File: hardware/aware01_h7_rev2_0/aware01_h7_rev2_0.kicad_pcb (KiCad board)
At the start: 4 copper layers, 46 x 110 mm, 161 parts, among them IC1 TLV320AIC3204IRHBR, IC2 587-2054-127F, IC3 587-2054-127F, IC4 587-2054-127F, IC5 587-2054-127F, J1 CV3_IN, J10 CV2_IN, J11 V/OCT_IN, J12 CV1_IN, J13 GATE3_IN, J14 GATE4_IN, J2 Conn_02x07_Odd_Even, J3 Conn_02x05_Odd_Even, J4 InL, J5 InR, J6 OutL, J7 OutR, J8 GATE1_IN, J9 GATE2_IN, Q1 MMBT3904, Q2 MMBT3904, Q3 MMBT3904, Q4 MMBT3904, SW2 SW_Push, SW3 SW_Push, U1 LMR50410Y5FQDBVRQ1, U10 NE5532DRG4, U11 LMV722IDR, U12 LMV722IDR, U2 STM32H7A3RITx, U3 10k, U4 10k, U5 10k, U6 10k, U7 LM1117MP-3.3, U8 LM4040DIM3X-10, U9 NE5532DRG4, Y2 WE-XTAL 24.0MHz 50ppm

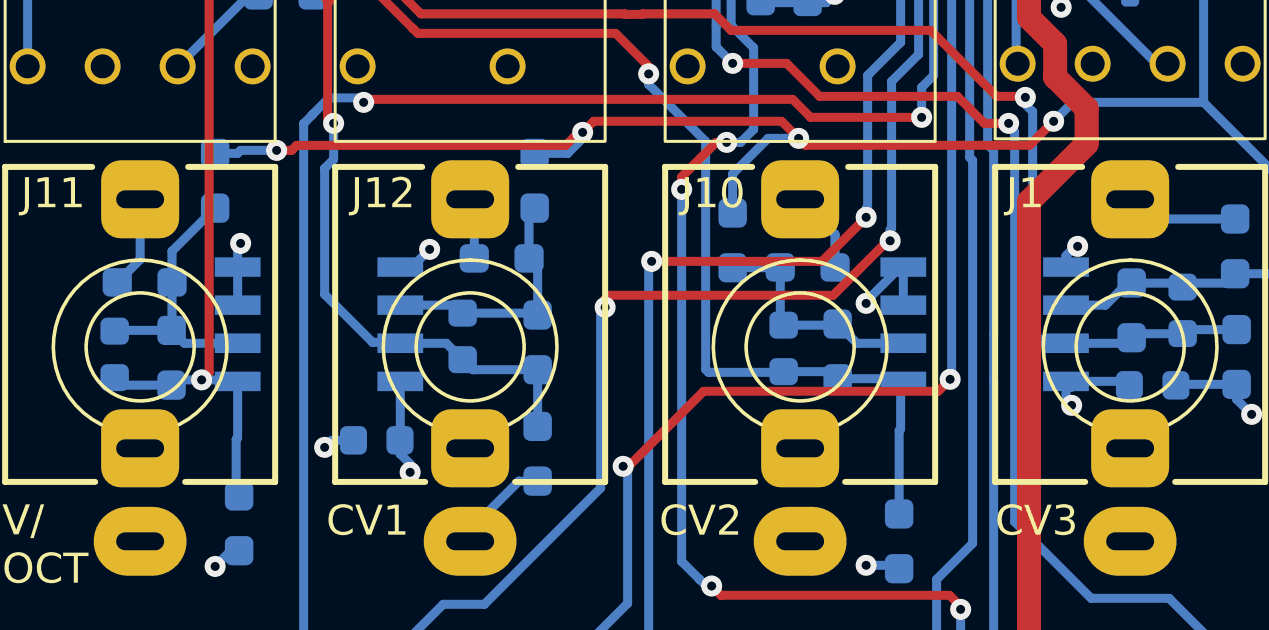
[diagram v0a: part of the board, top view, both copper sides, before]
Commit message: hwardware: update analog stages simulation
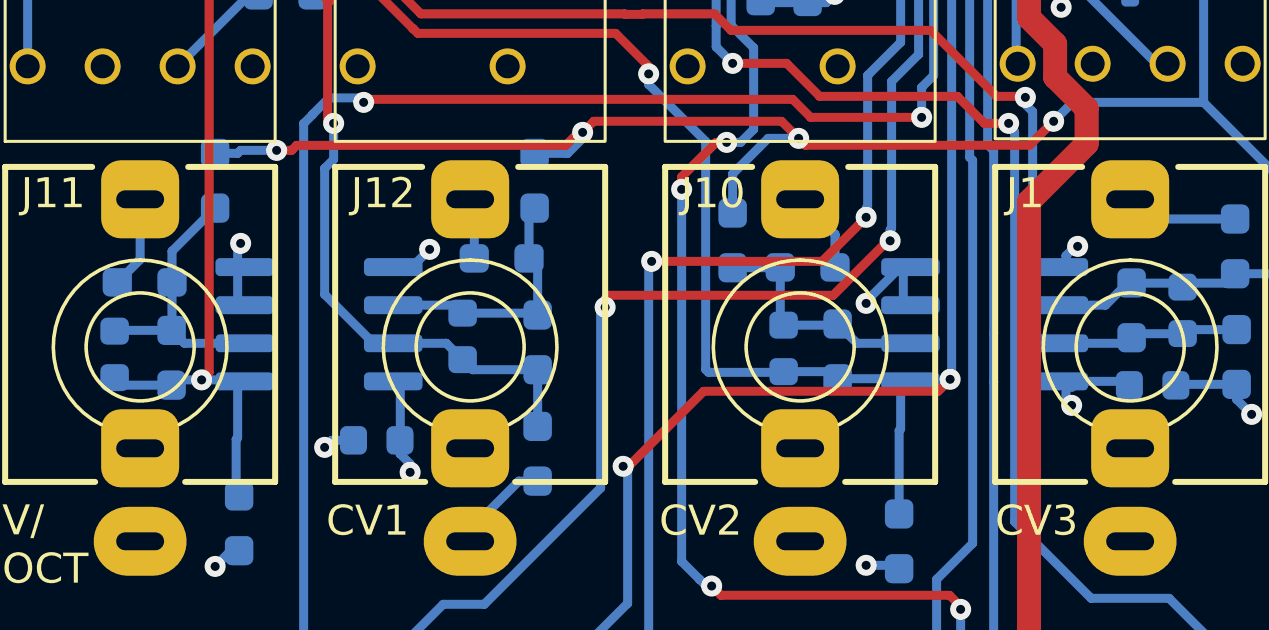
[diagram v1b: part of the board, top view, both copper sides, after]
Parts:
- U11, U12: value LMV722IDR -> OPA2322AIDR; footprint Eurorack:LMV722IDR -> Package_SO:SOIC-8_3.9x4.9mm_P1.27mm

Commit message: hardware: update analog sim and routing (wip)
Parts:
- removed the C50 at (137.8, 146.4)
- removed the C51 at (147.2, 144.6)
- removed the C56 at (164.1, 136.1)
- removed the C57 at (173.5, 136.1)
- removed the C58 at (159.4, 145.7)
- removed the C59 at (168.8, 144.3)
- removed the R11 at (173.2, 113.6)
- removed R48, R49, R58, R59: 22k, Resistor_SMD:R_0603_1608Metric_Pad0.98x0.95mm_HandSolder
- removed R50, R51, R56, R57: 3.3k, Resistor_SMD:R_0603_1608Metric_Pad0.98x0.95mm_HandSolder
- removed R52, R53, R60, R61: 1k, Resistor_SMD:R_0603_1608Metric_Pad0.98x0.95mm_HandSolder
- removed R54, R55, R69, R76, R77: 100k, Resistor_SMD:R_0603_1608Metric_Pad0.98x0.95mm_HandSolder
- added C49: 2.2u, Capacitor_SMD:CP_Elec_4x5.4, B.Cu at (153.7, 133.8)
- added C5: 10u, Capacitor_SMD:C_0603_1608Metric, B.Cu at (121.0, 136.7)
- added C52: 10u, Capacitor_SMD:CP_Elec_4x5.4, B.Cu at (164.1, 136.1)
- added C54: 18p, Capacitor_SMD:C_0603_1608Metric, B.Cu at (120.8, 120.0)
- added C55: 18p, Capacitor_SMD:C_0603_1608Metric, B.Cu at (117.8, 116.5)
- added C9: 10u, Capacitor_SMD:C_0603_1608Metric, B.Cu at (121.0, 139.2)
- added D4: BAT54S, Package_TO_SOT_SMD:SOT-23, B.Cu at (142.4, 138.8)
- added D5: BAT54S, Package_TO_SOT_SMD:SOT-23, B.Cu at (153.8, 139.3)
- added D6: BAT54A, Package_TO_SOT_SMD:SOT-23, B.Cu at (141.3, 127.7)
- added D7: BAT54A, Package_TO_SOT_SMD:SOT-23, B.Cu at (165.6, 129.9)
- added R14: 12k, Resistor_SMD:R_0603_1608Metric_Pad0.98x0.95mm_HandSolder, B.Cu at (114.9, 141.7)
- added R15: 12k, Resistor_SMD:R_0603_1608Metric_Pad0.98x0.95mm_HandSolder, B.Cu at (114.9, 136.7)
- added R16: 1.8k, Resistor_SMD:R_0603_1608Metric_Pad0.98x0.95mm_HandSolder, B.Cu at (114.9, 139.2)
- added R17: 1.8k, Resistor_SMD:R_0603_1608Metric_Pad0.98x0.95mm_HandSolder, B.Cu at (114.9, 134.2)
- added R18: 5.6k, Resistor_SMD:R_0603_1608Metric_Pad0.98x0.95mm_HandSolder, B.Cu at (118.1, 125.3)
- added R19: 5.6k, Resistor_SMD:R_0603_1608Metric_Pad0.98x0.95mm_HandSolder, B.Cu at (115.8, 116.9)
- added R20: 39k, Resistor_SMD:R_0603_1608Metric_Pad0.98x0.95mm_HandSolder, B.Cu at (120.8, 124.4)
- added R21: 39k, Resistor_SMD:R_0603_1608Metric_Pad0.98x0.95mm_HandSolder, B.Cu at (116.7, 114.0)
- added R22: 1k, Resistor_SMD:R_0603_1608Metric_Pad0.98x0.95mm_HandSolder, B.Cu at (121.9, 127.0)
- added R23: 1k, Resistor_SMD:R_0603_1608Metric_Pad0.98x0.95mm_HandSolder, B.Cu at (108.8, 107.5)
- added U3: LM1117MP-1.8, Package_TO_SOT_SMD:SOT-223-3_TabPin2, B.Cu at (153.2, 147.2)
- C53: value 2.2u -> 10u
- moved C53 19.8 mm to (173.3, 136.3), turned to -90 degrees
- moved R28 5.05 mm to (139.8, 123.5), turned to 90 degrees
- moved C48 2.83 mm to (142.3, 133.2), turned to -90 degrees
- moved R31 2.68 mm to (166.1, 126.0), turned to 0 degrees
- renumbered C18 to C1, C7 to C10, C38 to C11, C39 to C12, C25 to C13, C20 to C14, C21 to C15, C24 to C16, C12 to C17, C26 to C18, C1 to C19, C6 to C2, C10 to C20, C13 to C21, C29 to C22, C2 to C23, C14 to C24, C11 to C25, C40 to C26, C32 to C27, C16 to C28, C17 to C29, C19 to C3, C31 to C30, C34 to C31, C3 to C32, C5 to C33, C35 to C34, C27 to C35, C28 to C36, C41 to C37, C42 to C38, C43 to C39, C30 to C4, C44 to C40, C45 to C41, C46 to C42, C8 to C43, C9 to C44, C47 to C45, C48 to C46, C49 to C47, C52 to C48, C54 to C50, C55 to C51, C60 to C56, C61 to C57, C15 to C58, C62 to C59, C22 to C6, C63 to C60, C64 to C61, C23 to C7, C33 to C8, D3 to D1, D1 to D2, D2 to D3, IC5 to IC1, IC4 to IC2, IC2 to IC4, IC1 to IC5, J2 to J1, J14 to J10, J10 to J11, J1 to J12, J11 to J13, J12 to J14, J3 to J2, J4 to J3, J5 to J4, J6 to J5, J7 to J6, J8 to J7, J9 to J8, J13 to J9, L2 to L1, R46 to R1, R42 to R10, R43 to R11, R44 to R12, R45 to R13, R3 to R2, R62 to R24, R63 to R25, R78 to R26, R12 to R27, R64 to R28, R65 to R29, R2 to R3, R79 to R30, R13 to R31, R66 to R32, R67 to R33, R8 to R34, R9 to R35, R68 to R36, R10 to R37, R70 to R38, R71 to R39, R1 to R4, R72 to R40, R73 to R41, R74 to R42, R75 to R43, R80 to R5, R81 to R6, R47 to R7, R40 to R8, R41 to R9, SW2 to SW1, SW3 to SW2, TP5 to TP1, TP4 to TP2, TP2 to TP4, TP1 to TP5, U9 to U10, U10 to U11, U11 to U12, U12 to U13, U7 to U2, U2 to U4, U8 to U5, U3 to U6, U4 to U7, U5 to U8, U6 to U9, Y2 to Y1
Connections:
- C48 pad 1: Net-(C50-Pad1) -> /Audio Codec/Input Output Channels/INL
- C48 pad 2: /Audio Codec/Input Output Channels/INL -> Net-(C48-Pad2)
- C53 pad 1: Net-(C51-Pad1) -> /Audio Codec/Input Output Channels/OUTR
- C53 pad 2: /Audio Codec/Input Output Channels/INR -> Net-(C53-Pad2)
- J3 pad T: Net-(J4-PadT) -> Net-(U10A-+)
- J4 pad T: Net-(J5-PadT) (its old number) -> Net-(U10B-+)
- J4 pad TN: Net-(J4-PadT) -> Net-(U10A-+)
- U10 pad 1: Net-(C50-Pad1) -> Net-(U10A--)
- U10 pad 2: Net-(U9A--) -> Net-(U10A--)
- U10 pad 3: GND -> Net-(U10A-+)
- U10 pad 5: GND -> Net-(U10B-+)
- U10 pad 6: Net-(U9B--) -> Net-(U10B--)
- U10 pad 7: Net-(C51-Pad1) -> Net-(U10B--)
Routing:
- net Net-(U10A-+): track 0.00 -> 19.8 mm
- net Net-(J4-PadT): track 19.8 -> 0.00 mm
- net Net-(C51-Pad1): track 15.3 -> 0.00 mm
- net Net-(C50-Pad1): track 15.2 -> 0.00 mm
- net Net-(C56-Pad1): track 14.3 -> 0.00 mm
- net Net-(U10A--): track 0.00 -> 11.9 mm
- net Net-(C52-Pad2): track 0.00 -> 10.5 mm
- net Net-(U10B--): track 0.00 -> 10.3 mm
- net Net-(Q3-B): track 2.30 -> 10.9 mm, vias 0 -> 2
- net Net-(U12B--): track 7.94 -> 0.00 mm
- net Net-(U11B--): track 5.81 -> 13.7 mm
- net Net-(C57-Pad1): track 6.18 -> 0.00 mm
- net Net-(C53-Pad2): track 0.00 -> 6.18 mm
- net Net-(U9A--): track 5.79 -> 0.00 mm
- net Net-(U9B--): track 5.60 -> 0.00 mm
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
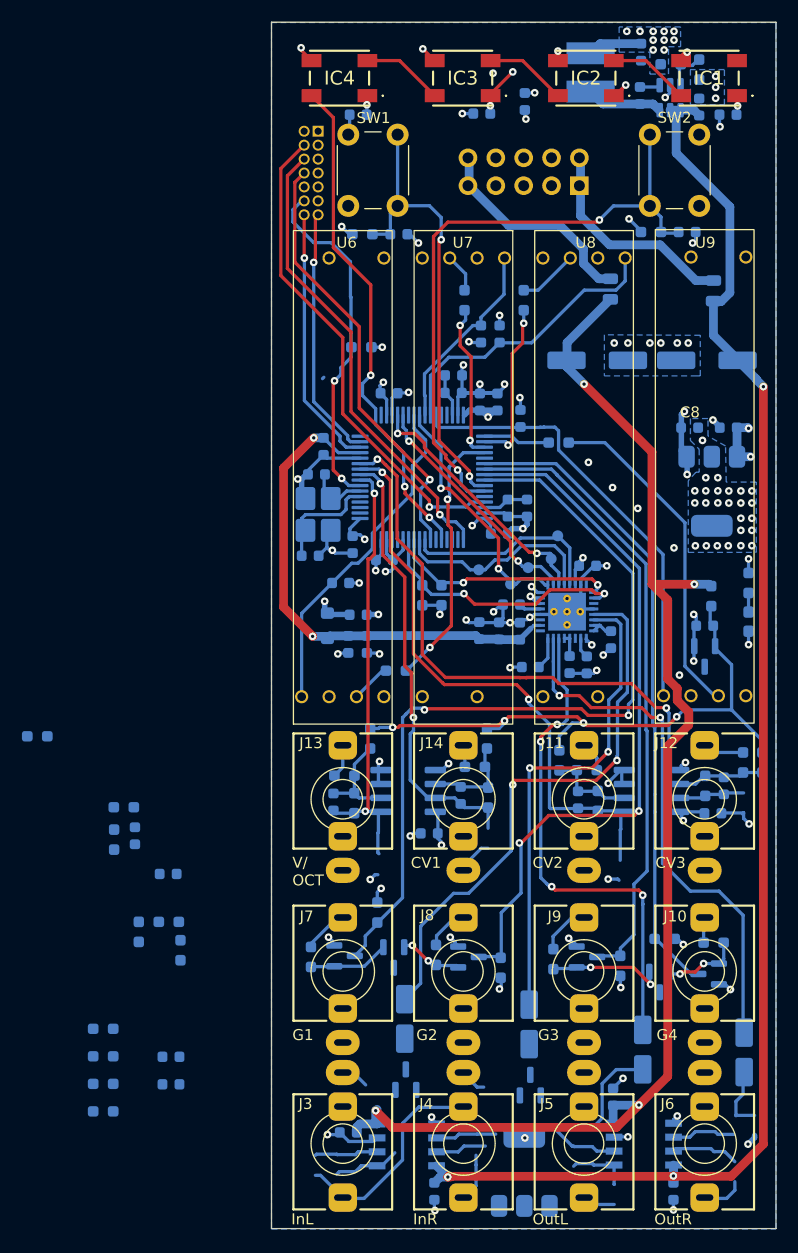
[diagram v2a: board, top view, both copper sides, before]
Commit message: hardware: update layout
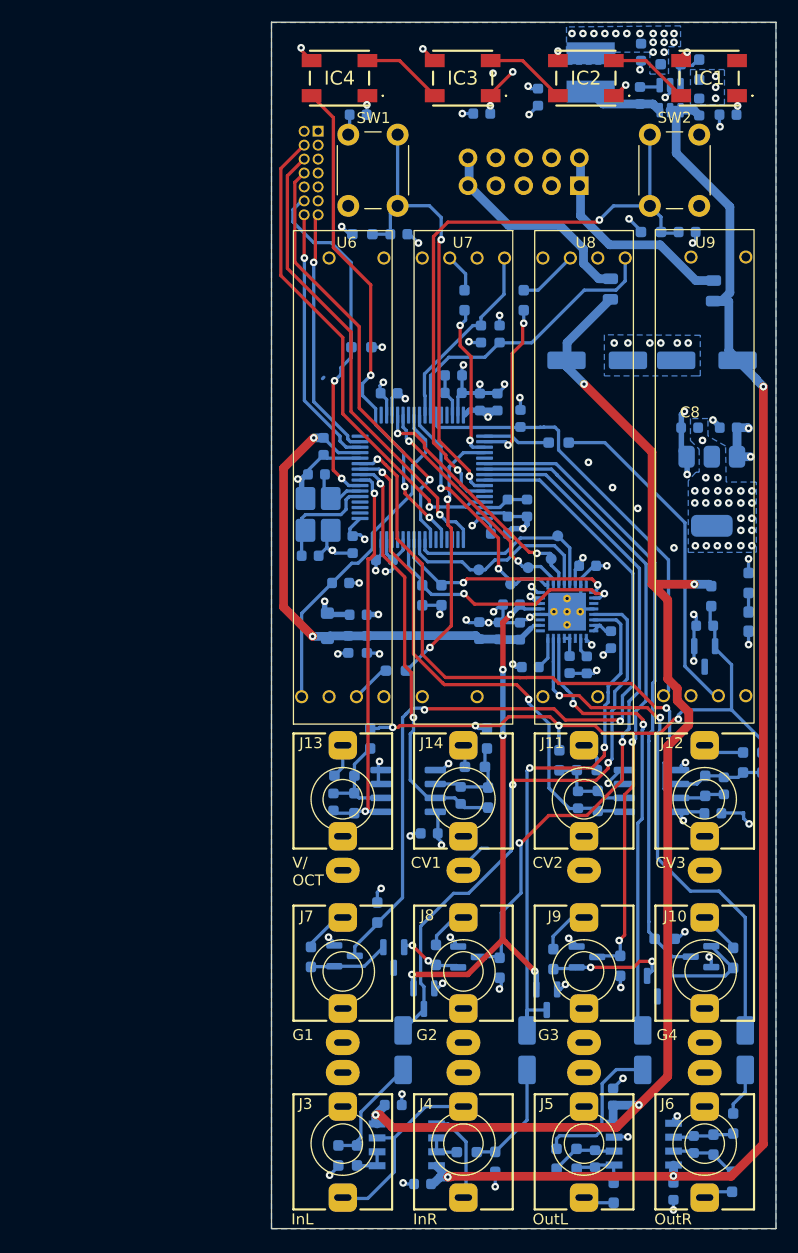
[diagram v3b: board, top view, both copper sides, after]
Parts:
- removed C5, C9: 10u, Capacitor_SMD:C_0603_1608Metric
- removed U3: LM1117MP-1.8, Package_TO_SOT_SMD:SOT-223-3_TabPin2
- moved R23 75.3 mm to (172.2, 148.1), turned to -90 degrees
- moved R19 62.1 mm to (172.3, 142.8), turned to -90 degrees
- moved R21 61.9 mm to (170.5, 144.7), turned to -90 degrees
- moved C55 58.2 mm to (168.7, 144.7), turned to -90 degrees
- moved C54 46.8 mm to (159.7, 146.0), turned to -90 degrees
- moved R22 45.3 mm to (161.4, 149.1)
- moved R18 43.7 mm to (157.1, 145.1), turned to 0 degrees
- moved R20 42.7 mm to (157.1, 146.9)
- moved R17 37.7 mm to (150.6, 146.3), turned to 90 degrees
- moved R15 34.3 mm to (148.0, 145.4)
- moved R14 23.5 mm to (138.0, 145.7), turned to 90 degrees
- moved R16 22.4 mm to (136.3, 145.7), turned to 90 degrees
- moved D5 7.93 mm to (155.3, 131.5), turned to -90 degrees
- moved D4 7.57 mm to (144.1, 131.4), turned to -90 degrees
- moved C47 4.80 mm to (141.3, 141.1), turned to 0 degrees
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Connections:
- C38 pad 2: Net-(IC5-DVDD) -> DVDD
- D4 pad 1: +1V8 -> DVDD
- D5 pad 1: +1V8 -> DVDD
- IC5 pad 29: Net-(IC5-DVDD) -> DVDD
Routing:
- net DVDD: track 0.00 -> 49.9 mm, vias 0 -> 5
- net Net-(C48-Pad2): track 0.00 -> 10.4 mm
- net Net-(C49-Pad2): track 0.00 -> 10.4 mm
- net Net-(U10A--): track 11.9 -> 3.01 mm
- net Net-(U12B--): track 0.00 -> 8.17 mm
- net Net-(U11B--): track 13.7 -> 5.58 mm
- net GND: track 142.9 -> 135.3 mm, vias 75 -> 76
- net Net-(U10B--): track 10.3 -> 3.13 mm
- net /Audio Codec/Input Output Channels/INR: track 44.2 -> 50.2 mm
- net /CV2_IN: track 54.1 -> 48.8 mm
- net +5V: track 20.5 -> 15.6 mm, vias 18 -> 23
- net /V_OCT_IN: track 39.9 -> 36.0 mm
- net Net-(U10B-+): track 4.73 -> 8.55 mm, vias 1 -> 0
- net /Audio Codec/Input Output Channels/OUTL: track 45.9 -> 42.2 mm, vias 4 -> 2
- net Net-(C52-Pad2): track 10.5 -> 13.8 mm
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
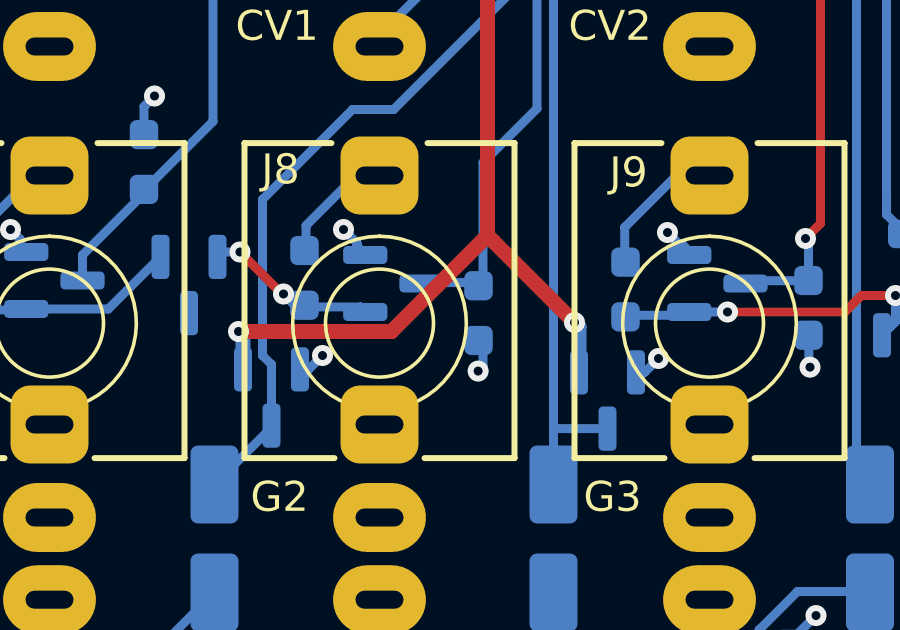
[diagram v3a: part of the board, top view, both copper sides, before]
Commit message: hardware: fix clamping diode orientation
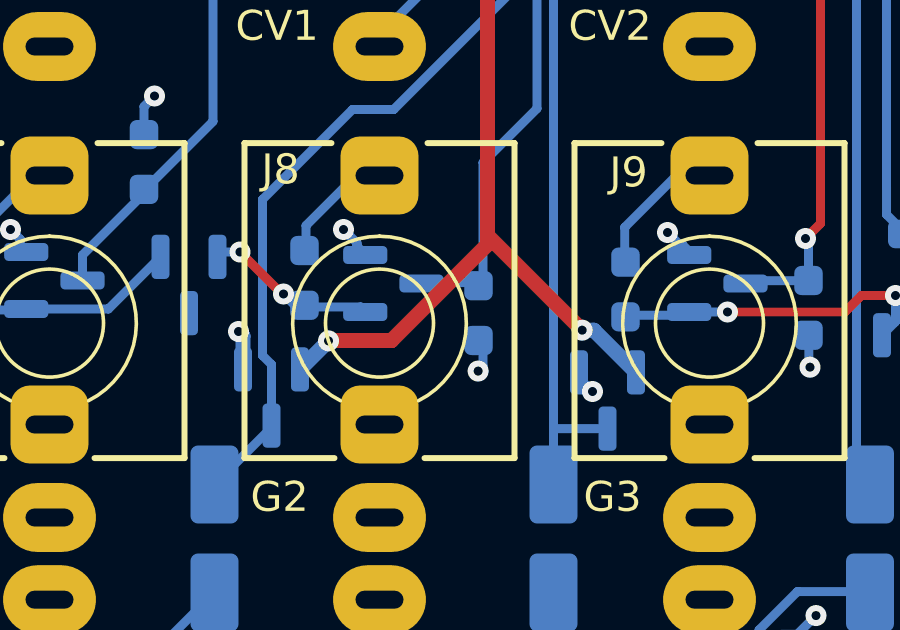
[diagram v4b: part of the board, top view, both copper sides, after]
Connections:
- D4 pad 1: DVDD -> GND
- D4 pad 2: GND -> DVDD
- D5 pad 1: DVDD -> GND
- D5 pad 2: GND -> DVDD
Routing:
- net DVDD: track 49.9 -> 48.3 mm
